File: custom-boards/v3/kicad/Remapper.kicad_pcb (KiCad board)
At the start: 2 copper layers, 15 x 32.8 mm, 30 parts, among them SW102 SW_Push, U103 RP2040, U105 W25Q128JVS, U4 TLV73333PDBV, Y101 Crystal_GND24

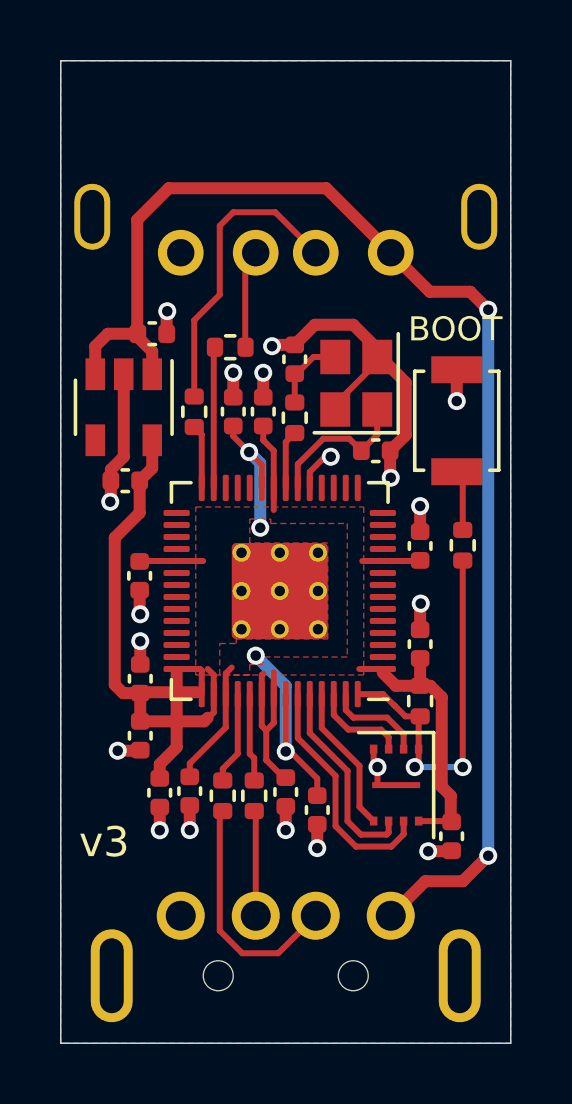
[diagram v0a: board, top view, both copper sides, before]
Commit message: Update custom boards
This commit makes the following changes to the custom PCB designs.

v1-v5: flash chip footprint changed, previous one caused issues in
manufacturing. Some other components moved around as a result.

v1-v5: flash chip changed from 1 megabyte to 2 megabyte one.

v1: USB Type A port component changed, previous one was consistently
soldered on crooked by JLCPCB.

The new designs are named v1.1-v5.1.

Schematics and enclosure files are unchanged.
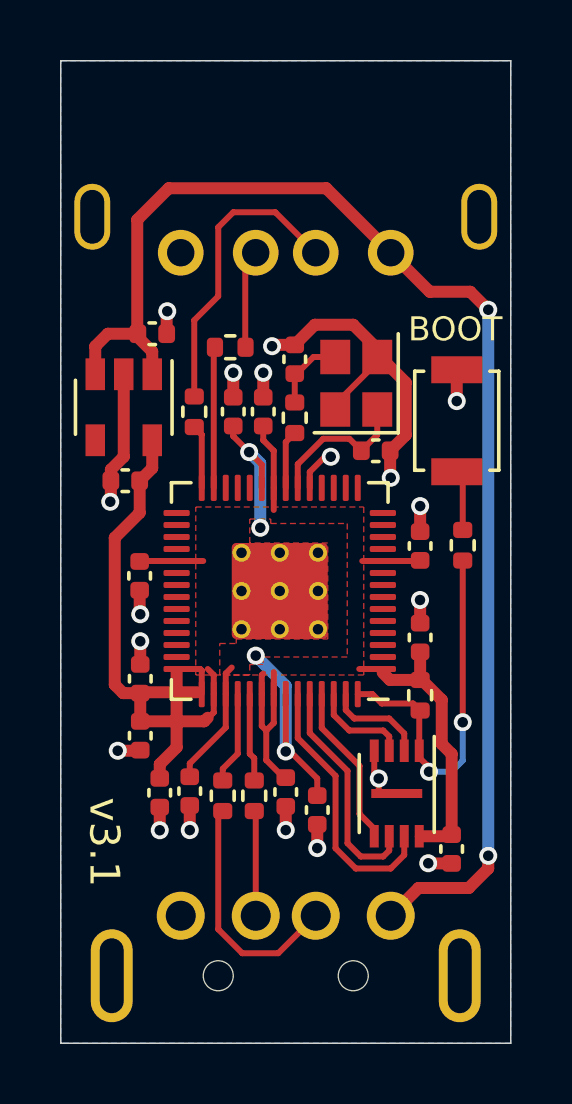
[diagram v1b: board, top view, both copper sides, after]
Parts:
- moved C117 0.42 mm to (152.0, 56.2)
- moved U105 0.28 mm to (150.2, 54.3)
- moved C104 0.22 mm to (151.0, 49.1)
- moved R105 0.20 mm to (151.0, 51.0)
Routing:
- net 1QSPI_SD3: track 8.08 -> 9.04 mm
- net 1QSPI_SCLK: track 6.72 -> 7.62 mm
- net 1QSPI_SD0: track 4.95 -> 5.46 mm
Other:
- board text added: "v3.1"
- board text removed: "v3"

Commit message: Add an LED to v3
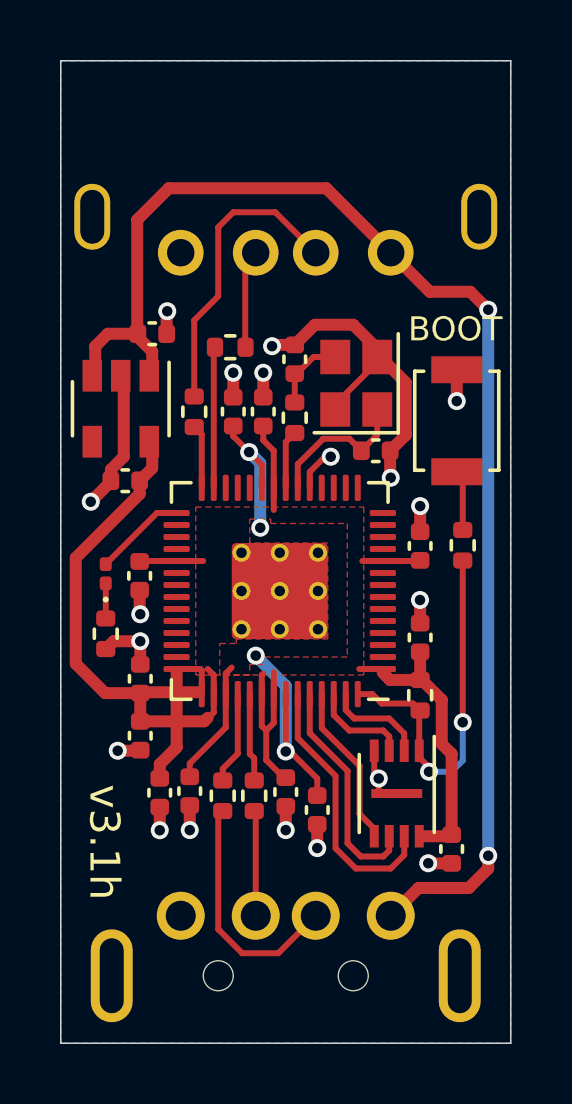
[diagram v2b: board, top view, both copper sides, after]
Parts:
- added D1: LED, LED_SMD:LED_0201_0603Metric, F.Cu at (140.5, 47.0)
- added R108: 300, Resistor_SMD:R_0402_1005Metric, F.Cu at (140.5, 49.0)
- moved U4 0.11 mm to (141.0, 41.5)
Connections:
- U103 pad 29: unconnected-(U103-GPIO18-Pad29) -> L0
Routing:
- net L0: track 0.00 -> 3.07 mm
- net GND: track 30.1 -> 31.7 mm
- net +3V3: track 44.7 -> 46.1 mm
- net Net-(D1-K): track 0.00 -> 1.17 mm
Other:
- board text added: "v3.1h"
- board text removed: "v3.1"

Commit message: Use a cheaper type of LED
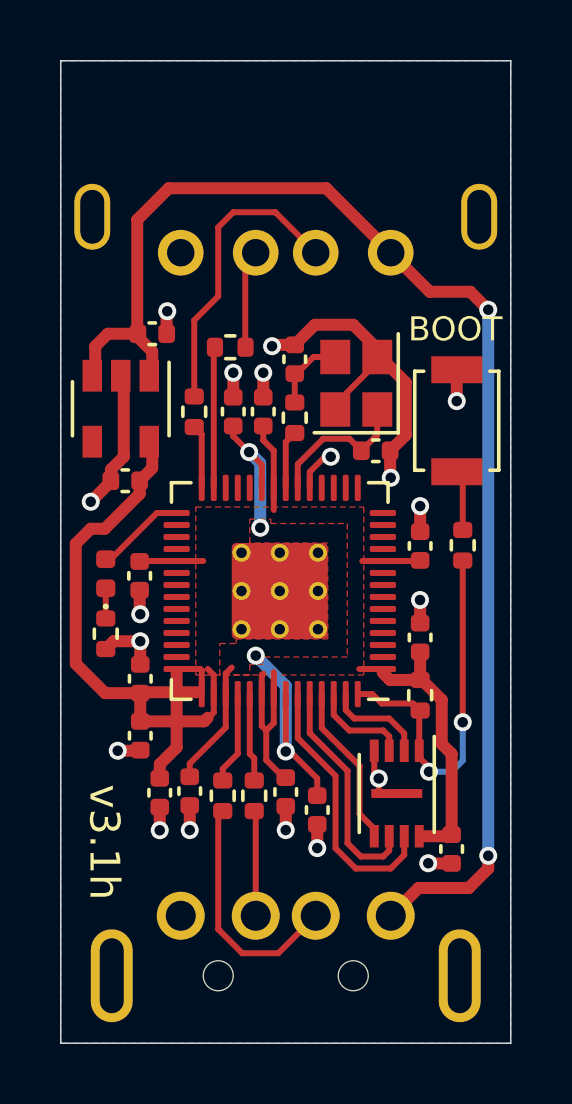
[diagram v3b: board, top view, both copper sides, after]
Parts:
- D1: footprint LED_SMD:LED_0201_0603Metric -> LED_SMD:LED_0402_1005Metric
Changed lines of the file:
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@@
 		)
 	)
-	(footprint "LED_SMD:LED_0201_0603Metric"
+	(footprint "LED_SMD:LED_0402_1005Metric"
 		(layer "F.Cu")
 		(at 140.5 47 90)
-		(descr "LED SMD 0201 (0603 Metric), square (rectangular) end terminal, IPC_7351 nominal, (Body size source: https://www.vishay.com/docs/20052/crcw0201e3.pdf), generated with kicad-footprint-generator")
+		(descr "LED SMD 0402 (1005 Metric), square (rectangular) end terminal, IPC_7351 nominal, (Body size source: http://www.tortai-tech.com/upload/download/2011102023233369053.pdf), generated with kicad-footprint-generator")
 		(tags "LED")
 		(property "Reference" "D1"
-			(at 0 -1.05 90)
+			(at 0 -1.17 90)
 			(layer "F.SilkS")
 			(hide yes)
@@
 		)
 		(property "Value" "LED"
-			(at 0 1.05 90)
+			(at 0 1.17 90)
 			(layer "F.Fab")
 			(effects
@@
 			)
 		)
-		(property "Footprint" "LED_SMD:LED_0201_0603Metric"
+		(property "Footprint" "LED_SMD:LED_0402_1005Metric"
 			(at 0 0 90)
 			(unlocked yes)
@@
 			)
 		)
+		(property "LCSC" "C130725"
+			(at 0 0 0)
+			(layer "F.SilkS")
+			(hide yes)
+			(effects
+				(font
+					(size 1.27 1.27)
+					(thickness 0.15)
+				)
+			)
+		)
 		(property ki_fp_filters "LED* LED_SMD:* LED_THT:*")
 		(sheetname "Root")
@@
 		(attr smd)
 		(fp_circle
-			(center -0.86 0)
-			(end -0.81 0)
+			(center -1.09 0)
+			(end -1.04 0)
 			(stroke
 				(width 0.1)
@@
 		)
 		(fp_line
-			(start 0.7 -0.35)
-			(end 0.7 0.35)
+			(start 0.93 -0.47)
+			(end 0.93 0.47)
 			(stroke
 				(width 0.05)
@@
 		)
 		(fp_line
-			(start -0.7 -0.35)
-			(end 0.7 -0.35)
+			(start -0.93 -0.47)
+			(end 0.93 -0.47)
 			(stroke
 				(width 0.05)
@@
 		)
 		(fp_line
-			(start 0.7 0.35)
-			(end -0.7 0.35)
+			(start 0.93 0.47)
+			(end -0.93 0.47)
 			(stroke
 				(width 0.05)
@@
 		)
 		(fp_line
-			(start -0.7 0.35)
-			(end -0.7 -0.35)
+			(start -0.93 0.47)
+			(end -0.93 -0.47)
 			(stroke
 				(width 0.05)
@@
 		)
 		(fp_line
-			(start 0.3 -0.15)
-			(end 0.3 0.15)
+			(start 0.5 -0.25)
+			(end 0.5 0.25)
 			(stroke
 				(width 0.1)
@@
 		)
 		(fp_line
-			(start -0.3 -0.15)
-			(end 0.3 -0.15)
+			(start -0.5 -0.25)
+			(end 0.5 -0.25)
 			(stroke
 				(width 0.1)
@@
 		)
 		(fp_line
-			(start 0.3 0.15)
-			(end -0.3 0.15)
+			(start 0.5 0.25)
+			(end -0.5 0.25)
 			(stroke
 				(width 0.1)
@@
 		)
 		(fp_line
-			(start -0.1 0.15)
-			(end -0.1 -0.15)
+			(start -0.3 0.25)
+			(end -0.3 -0.25)
 			(stroke
 				(width 0.1)
@@
 		)
 		(fp_line
-			(start -0.2 0.15)
-			(end -0.2 -0.15)
+			(start -0.4 0.25)
+			(end -0.4 -0.25)
 			(stroke
 				(width 0.1)
@@
 		)
 		(fp_line
-			(start -0.3 0.15)
-			(end -0.3 -0.15)
+			(start -0.5 0.25)
+			(end -0.5 -0.25)
 			(stroke
 				(width 0.1)
@@
 		)
 		(fp_text user "${REFERENCE}"
-			(at 0 -0.68 90)
+			(at 0 0 90)
 			(layer "F.Fab")
 			(effects
@@
 			)
 		)
-		(pad "" smd roundrect
-			(at -0.345 0 90)
-			(size 0.318 0.36)
-			(layers "F.Paste")
-			(roundrect_rratio 0.25)
-		)
-		(pad "" smd roundrect
-			(at 0.345 0 90)
-			(size 0.318 0.36)
-			(layers "F.Paste")
-			(roundrect_rratio 0.25)
-		)
 		(pad "1" smd roundrect
-			(at -0.32 0 90)
-			(size 0.46 0.4)
-			(layers "F.Cu" "F.Mask")
+			(at -0.485 0 90)
+			(size 0.59 0.64)
+			(layers "F.Cu" "F.Paste" "F.Mask")
 			(roundrect_rratio 0.25)
 			(net 55 "Net-(D1-K)")
@@
 		)
 		(pad "2" smd roundrect
-			(at 0.32 0 90)
-			(size 0.46 0.4)
-			(layers "F.Cu" "F.Mask")
+			(at 0.485 0 90)
+			(size 0.59 0.64)
+			(layers "F.Cu" "F.Paste" "F.Mask")
 			(roundrect_rratio 0.25)
 			(net 22 "L0")
@@
 			(pintype "passive")
 		)
-		(model "${KICAD8_3DMODEL_DIR}/LED_SMD.3dshapes/LED_0201_0603Metric.wrl"
+		(model "${KICAD8_3DMODEL_DIR}/LED_SMD.3dshapes/LED_0402_1005Metric.wrl"
 			(offset
 				(xyz 0 0 0)
@@
 	)
 	(segment
-		(start 141.65 50.98)
-		(end 140.48 50.98)
-		(width 0.4)
-		(layer "F.Cu")
-		(net 5)
-	)
-	(segment
 		(start 145.85 53.213004)
 		(end 146.431996 53.795)
@@
 	)
 	(segment
-		(start 141.63 43.9)
-		(end 142.05 43.48)
+		(start 139.5 50)
+		(end 139.5 46)
 		(width 0.4)
 		(layer "F.Cu")
@@
 	)
 	(segment
-		(start 144.1 50.375)
-		(end 143.9 50.175)
-		(width 0.2)
-		(layer "F.Cu")
-		(net 5)
-	)
-	(segment
-		(start 139.5 46.47)
-		(end 141.63 44.34)
+		(start 141.63 43.9)
+		(end 142.05 43.48)
 		(width 0.4)
 		(layer "F.Cu")
@@
 	)
 	(segment
-		(start 141.63 44.34)
-		(end 141.63 43.9)
-		(width 0.4)
+		(start 144.1 50.375)
+		(end 143.9 50.175)
+		(width 0.2)
 		(layer "F.Cu")
 		(net 5)
@@
 	)
 	(segment
-		(start 139.5 50)
-		(end 139.5 46.47)
-		(width 0.4)
-		(layer "F.Cu")
-		(net 5)
-	)
-	(segment
 		(start 146.1 51.0125)
 		(end 146.1 50.275)
@@
 	)
 	(segment
-		(start 140.48 50.98)
-		(end 139.5 50)
+		(start 141.63 44.34)
+		(end 141.63 43.9)
 		(width 0.4)
 		(layer "F.Cu")
@@
 	)
 	(segment
+		(start 141.65 50.98)
+		(end 140.48 50.98)
+		(width 0.4)
+		(layer "F.Cu")
+		(net 5)
+	)
+	(segment
 		(start 151.7 51.203396)
 		(end 151.7 52.675)
@@
 	)
 	(segment
+		(start 140.48 50.98)
+		(end 139.5 50)
+		(width 0.4)
+		(layer "F.Cu")
+		(net 5)
+	)
+	(segment
 		(start 142.3 53.82)
 		(end 142.3 53.35)
@@
 	)
 	(segment
+		(start 140.47 45.5)
+		(end 141.63 44.34)
+		(width 0.4)
+		(layer "F.Cu")
+		(net 5)
+	)
+	(segment
 		(start 141.68 50.95)
 		(end 143.55 50.95)
@@
 	)
 	(segment
+		(start 140 45.5)
+		(end 140.47 45.5)
+		(width 0.4)
+		(layer "F.Cu")
+		(net 5)
+	)
+	(segment
 		(start 151.7 52.675)
 		(end 152.03 53.005)
@@
 		(layer "F.Cu")
 		(net 5)
+	)
+	(segment
+		(start 139.5 46)
+		(end 140 45.5)
+		(width 0.4)
+		(layer "F.Cu")
+		(net 5)

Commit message: Use GPIO 19 instead of 18
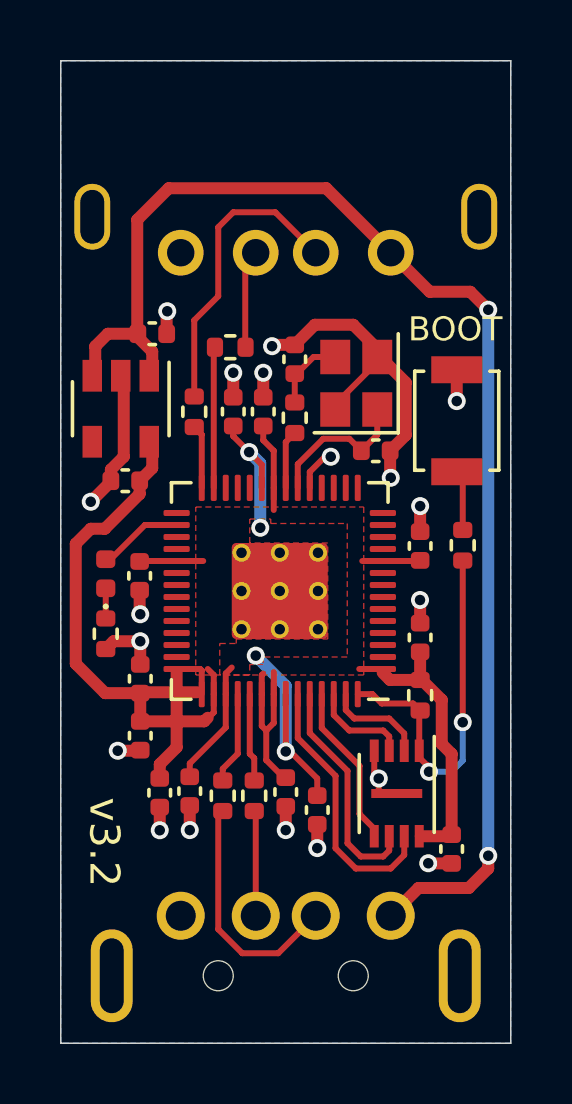
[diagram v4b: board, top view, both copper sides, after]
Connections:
- U103 pad 29: L0 -> unconnected-(U103-GPIO18-Pad29)
- U103 pad 30: unconnected-(U103-GPIO19-Pad30) -> L0
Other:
- board text added: "v3.2"
- board text removed: "v3.1h"
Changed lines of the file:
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@@
 	(net 21 "unconnected-(U103-RUN-Pad26)")
 	(net 22 "L0")
-	(net 23 "unconnected-(U103-GPIO19-Pad30)")
+	(net 23 "unconnected-(U103-GPIO18-Pad29)")
 	(net 24 "unconnected-(U103-GPIO20-Pad31)")
 	(net 25 "unconnected-(U103-GPIO21-Pad32)")
@@
 			(layers "F.Cu" "F.Paste" "F.Mask")
 			(roundrect_rratio 0.25)
-			(net 22 "L0")
+			(net 23 "unconnected-(U103-GPIO18-Pad29)")
 			(pinfunction "GPIO18")
-			(pintype "bidirectional")
+			(pintype "bidirectional+no_connect")
 		)
 		(pad "30" smd roundrect
@@
 			(layers "F.Cu" "F.Paste" "F.Mask")
 			(roundrect_rratio 0.25)
-			(net 23 "unconnected-(U103-GPIO19-Pad30)")
+			(net 22 "L0")
 			(pinfunction "GPIO19")
-			(pintype "bidirectional+no_connect")
+			(pintype "bidirectional")
 		)
 		(pad "31" smd roundrect
@@
 		)
 	)
-	(gr_text "v3.1h"
+	(gr_text "v3.2"
 		(at 140.45 55.95 270)
 		(layer "F.SilkS")
@@
 	)
 	(segment
-		(start 142.205 44.975)
+		(start 141.805 45.375)
 		(end 140.5 46.68)
 		(width 0.2)
@@
 	)
 	(segment
-		(start 142.8625 44.975)
-		(end 142.205 44.975)
+		(start 142.8625 45.375)
+		(end 141.805 45.375)
 		(width 0.2)
 		(layer "F.Cu")
